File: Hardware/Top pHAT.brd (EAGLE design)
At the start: 85 x 56 mm, 41 parts, among them J1 QWIIC, J2 AVR_SPI_PROG_3X2TESTPOINTS, U1 RASPBERRY_PI_40BTM-NOHOLES, U2 ADMP401, U3 ADMP401, U4 WM8960, U5 ATTINY84

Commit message: pre design review for REDs
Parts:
- removed H5, H6: STAND-OFFTIGHT, SparkFun-Hardware:STAND-OFF-TIGHT
- removed U6: (no value), SparkFun-Displays:FPC05040-17204
- added C13: 10nF, SparkFun-Capacitors:0603
- added FD1, FD2, FD3, FD4: FIDUCIAL1X2, SparkFun-Aesthetics:FIDUCIAL-1X2
- added J3: 2.4" TFT, SparkFun-Displays:FPC05040-17204
- added LOGO1: SFE_LOGO_NAME_FLAME.1_INCH, SparkFun-Aesthetics:SFE_LOGO_NAME_FLAME_.1
- added LOGO2: SFE_LOGO_NAME_FLAME.4_INCH, SparkFun-Aesthetics:SFE_LOGO_NAME_FLAME_.4
- added LOGO3: QWIIC_LOGO_4MM, SparkFun-Aesthetics:QWIIC_4MM
- added LOGO4: OSHW-LOGOS, SparkFun-Aesthetics:OSHW-LOGO-S
- added Q2: 1.1A/60V/600mΩ, SparkFun-DiscreteSemi:SOT23-3
- added R4: 10k, SparkFun-Resistors:0603
- added TP1, TP10, TP11, TP12, TP13, TP14, TP15, TP2, TP3, TP4, TP5, TP6, TP7, TP8, TP9: TEST-POINT3X5, SparkFun-Connectors:PAD.03X.05
- added U$1: (no value), buzzard_labels (21):_TOP_PHAT1
- added U$2: (no value), buzzard_labels (21):TOP_PHAT0
- added U$4: (no value), buzzard_labels (16):02
- added U$5: (no value), buzzard_labels (16):53
- added U$6: (no value), buzzard_labels (16):A0
- added U$7: (no value), buzzard_labels (16):B1
- added U$8: (no value), buzzard_labels (17):I2C3
- added Y1: 24 MHz, SparkFun-Clocks:RESONATOR-SMD-3.2X2.5
- FRAME1: value FRAME-LETTER -> FRAME-LEDGER
- LS2: value SPEAKERCVS-1508 -> CVS-1508
- U1: value RASPBERRY_PI_40BTM-NOHOLES -> (none)
- moved J1 83.9 mm to (78.5, 5.00), turned to 0 degrees
- moved I2C 77.8 mm to (72.5, 5.00)
- moved R2 77.8 mm to (72.5, 1.50)
- moved R3 77.8 mm to (72.5, 3.00)
- moved FRAME1 12.0 mm to (12.0, -20.0)
- moved LS2 9.01 mm to (68.0, 27.5), turned to 180 degrees
- moved C1 5.07 mm to (68.0, 7.55), turned to 180 degrees
- moved C5 5.02 mm to (66.5, 47.5), turned to 0 degrees
- moved C12 4.00 mm to (73.5, 20.5)
- moved R1 4.00 mm to (73.5, 19.0)
- moved C8 3.16 mm to (77.5, 39.5), turned to 90 degrees
- moved C7 0.71 mm to (76.0, 39.5), turned to 90 degrees
- moved C6 0.50 mm to (72.0, 37.5)
- turned C4 to 180 degrees
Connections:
- net !RST renamed !RST_ATTINY
- removed net ADC-LRC: U4.15
- removed net INT: U5.6
- removed net N$31: J1.3, R2.1, U1.5
- removed net N$32: J1.4, R3.1, U1.3
- new net !BKLITE: Q2.1, TP12.P$1, U1.15
- new net !CS: J3.32, R4.1, TP6.P$1, U1.24
- new net !INT: TP15.P$1, U1.22, U5.6
- new net !RST_SCREEN: J3.34, TP13.P$1, U1.16
- new net D/C: J3.30, TP14.P$1, U1.18
- new net N$11: U4.11, Y1.3
- new net N$4: J3.8, Q2.3
- new net SCK: J3.33, TP5.P$1, U1.23
- new net SDI: J3.39, TP3.P$1, U1.19
- new net SDO: J3.28, TP4.P$1, U1.21
- net 3.3V: now also C13.1, J3.29, J3.31, J3.38, Q2.2, R4.2, Y1.1, Y1.4
- net ADC-DAT: now also TP10.P$1
- net BCLK: now also TP8.P$1
- net DAC-DAT: now also TP11.P$1
- net DAC-LRC: now also TP9.P$1, U4.15
- net GND: now also C13.2, J3.1, J3.11, J3.12, J3.13, J3.14, J3.15, J3.16, J3.17, J3.18, J3.19, J3.20, J3.21, J3.22, J3.23, J3.24, J3.25, J3.26, J3.27, J3.4, J3.40, J3.5, J3.6, J3.7, Y1.2
- net LED_DATA: now also TP7.P$1
- net SCL: now also J1.4, R2.1, TP1.P$1, U1.5
- net SDA: now also J1.3, R3.1, TP2.P$1, U1.3
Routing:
- net 3.3V: track 33.1 -> 194.1 mm, vias 1 -> 7
- net SDA: track 36.9 -> 175.1 mm, vias 1 -> 6
- net SCL: track 38.5 -> 170.3 mm, vias 1 -> 4
- net !INT: track 0.00 -> 67.6 mm, vias 0 -> 3
- net 5V: track 113.3 -> 163.7 mm, vias 1 -> 5
- net N$4: track 0.00 -> 49.0 mm, vias 0 -> 1
- net !BKLITE: track 0.00 -> 47.2 mm, vias 0 -> 3
- net !RST_SCREEN: track 0.00 -> 43.1 mm, vias 0 -> 2
- net !CS: track 0.00 -> 41.0 mm, vias 0 -> 3
- net D/C: track 0.00 -> 39.1 mm, vias 0 -> 4
- net SCK: track 0.00 -> 30.9 mm, vias 0 -> 2
- net SDO: track 0.00 -> 30.2 mm, vias 0 -> 2
- net N$31: track 23.1 -> 0.00 mm, vias 1 -> 0
- net SDI: track 0.00 -> 18.6 mm
- net N$32: track 16.7 -> 0.00 mm, vias 1 -> 0
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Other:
- board text added: "Andy England"
- board text added: "Units in mm"
- board text added: "v10"

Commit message: post design review
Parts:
- moved C11 5.68 mm to (68.0, 49.3)
- moved C2 1.27 mm to (72.0, 52.8)
- moved U3 1.27 mm to (67.0, 52.8)
- moved J3 1.00 mm to (19.0, 28.9)
- moved TP14 1.00 mm to (25.7, 31.8)
- moved TP3 1.00 mm to (21.9, 38.1)
- moved TP4 1.00 mm to (23.1, 31.8)
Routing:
- net MICBIAS: track 72.8 -> 71.0 mm
- net !RST_SCREEN: track 43.1 -> 44.5 mm
- net SCK: track 30.9 -> 32.3 mm
- net !CS: track 41.0 -> 42.4 mm
- net N$30: track 5.95 -> 7.22 mm
- net N$4: track 49.0 -> 50.0 mm
- net D/C: track 39.1 -> 40.1 mm
- net GND: vias 40 -> 42

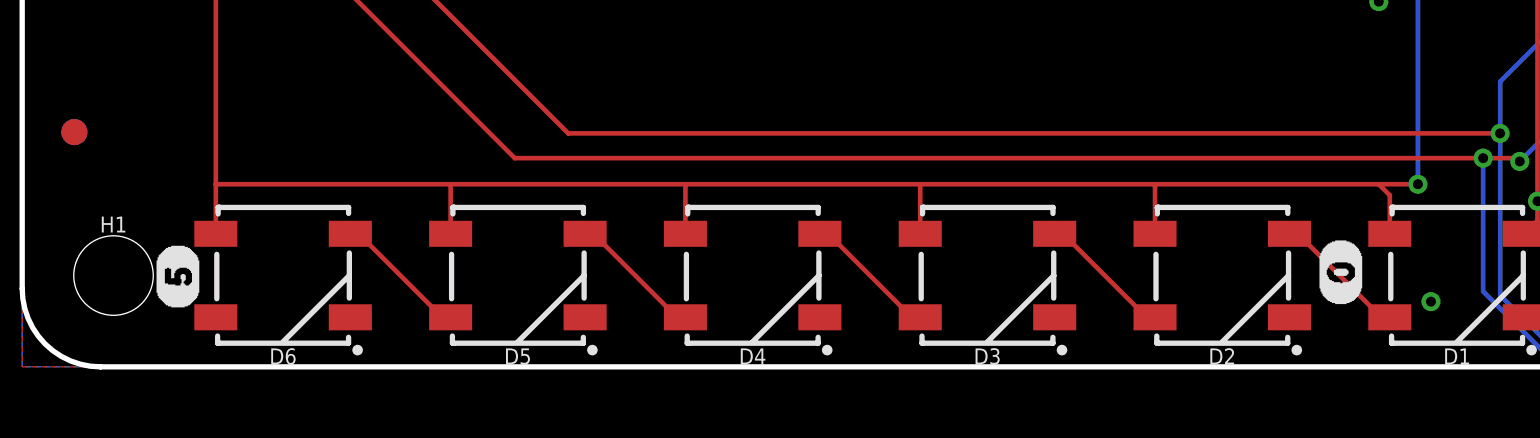
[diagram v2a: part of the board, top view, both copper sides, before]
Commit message: Adding LED numbers
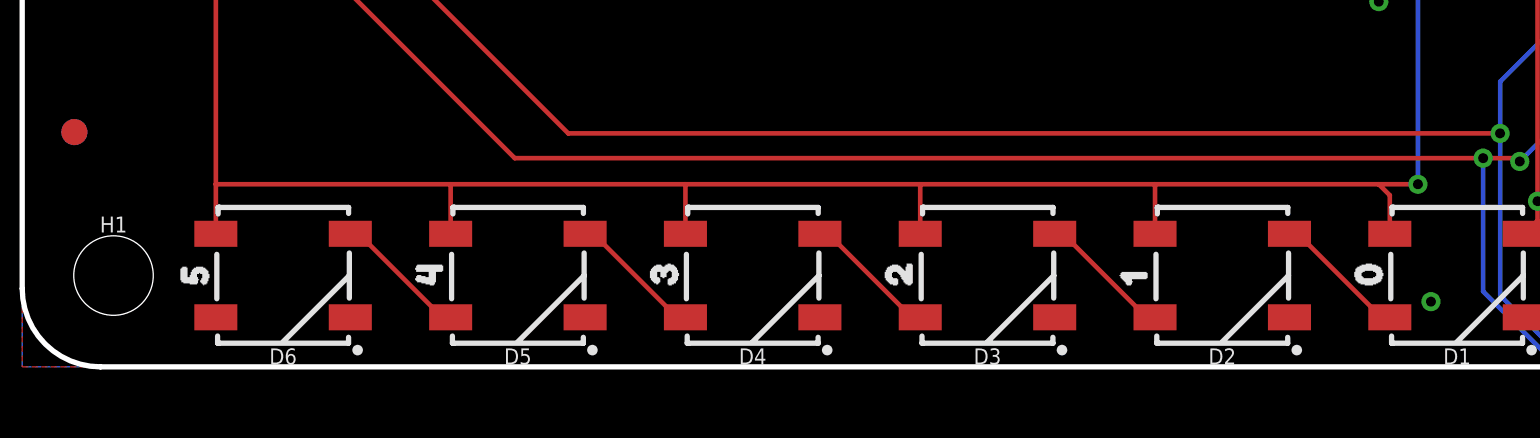
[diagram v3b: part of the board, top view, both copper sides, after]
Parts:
- added U$10: (no value), buzzard_labels (22):44
- added U$11: (no value), buzzard_labels (22):55
- added U$3: (no value), buzzard_labels (22):00
- added U$9: (no value), buzzard_labels (22):33
- U$4: device buzzard_labels (16):02 -> buzzard_labels (22):11
- U$5: device buzzard_labels (16):53 -> buzzard_labels (22):22
- moved U$5 27.6 mm to (33.6, 2.20)
- moved U$4 7.95 mm to (42.6, 2.20)
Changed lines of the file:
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@@
 <?xml version="1.0" encoding="utf-8"?>
 <!DOCTYPE eagle SYSTEM "eagle.dtd">
-<eagle version="9.3.1">
+<eagle version="9.5.2">
 <drawing>
 <settings>
@@
 <attribute name="VALUE" x="36.788" y="52.5" size="0.6096" layer="27" font="vector" ratio="20" rot="R270" align="top-center"/>
 </element>
-<element name="U$4" library="buzzard_labels (16)" package="02" value="" x="50.546" y="2.286" smashed="yes" rot="R90"/>
-<element name="U$5" library="buzzard_labels (16)" package="53" value="" x="5.969" y="2.159" smashed="yes" rot="R90"/>
 <element name="U$6" library="buzzard_labels (16)" package="A0" value="" x="80.899" y="32.766" smashed="yes" rot="R90"/>
 <element name="U$7" library="buzzard_labels (16)" package="B1" value="" x="81.026" y="51.181" smashed="yes" rot="R90"/>
@@
 <element name="TP14" library="SparkFun-Connectors" package="PAD.03X.05" value="TEST-POINT3X5" x="25.67" y="31.75" smashed="yes" rot="MR0"/>
 <element name="TP15" library="SparkFun-Connectors" package="PAD.03X.05" value="TEST-POINT3X5" x="59.69" y="19.05" smashed="yes" rot="MR0"/>
+<element name="U$3" library="buzzard_labels (22)" package="00" value="" x="51.6" y="2.2" smashed="yes" rot="R90"/>
+<element name="U$4" library="buzzard_labels (22)" package="11" value="" x="42.6" y="2.2" smashed="yes" rot="R90"/>
+<element name="U$5" library="buzzard_labels (22)" package="22" value="" x="33.6" y="2.2" smashed="yes" rot="R90"/>
+<element name="U$9" library="buzzard_labels (22)" package="33" value="" x="24.6" y="2.2" smashed="yes" rot="R90"/>
+<element name="U$10" library="buzzard_labels (22)" package="44" value="" x="15.6" y="2.2" smashed="yes" rot="R90"/>
+<element name="U$11" library="buzzard_labels (22)" package="55" value="" x="6.6" y="2.2" smashed="yes" rot="R90"/>
 </elements>
 <signals>
